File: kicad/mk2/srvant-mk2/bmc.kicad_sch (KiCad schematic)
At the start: 91 parts, among them J5 ARJM11, U13 KSZ9131RNXI-TR, U14 TPD4EUSB30, U15 TPD4EUSB30, Y2 25Mhz

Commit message: more progress
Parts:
- removed U12: ~, symbol custom-libraries:t113-s3
- added U4, U?: rp-t113-s3, rp-t113-s3:rp-t113-s3, symbol custom-libraries:t113-s3
- Y2: footprint srvant:LFXTAL-25MHz -> footprints:LFXTAL-25MHz; farnell# (none) -> 2854241; manf# (none) -> MCSJK-6F-25.00-20-30-40-B-50
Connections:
- net 3.3v: now also U4.30 (VCC-3V3)
- net EPHY_25M: now also U4.129 (EPHY_25M)
- net GND: now also U4.1 (GND), U4.105 (GND), U4.107 (GND), U4.109 (GND), U4.111 (GND), U4.114 (GND), U4.117 (GND), U4.134 (GND), U4.27 (GND), U4.29 (GND), U4.31 (GND), U4.33 (GND), U4.39 (GND), U4.56 (GND), U4.80 (GND), U4.87 (GND), U4.9 (GND), U4.90 (GND), U4.93 (GND), U4.99 (GND)
- net PHY_INT_N: now also U4.61 (PD_EINT4)
- net PHY_MDC: now also U4.119 (RMII-MDC)
- net PHY_MDIO: now also U4.118 (RMII-MDIO)
- net RESET_OUT_N: now also U4.60 (PD_EINT3)
- net RXC: now also U4.124 (RGMII_RXCK)
- net RXD0: now also U4.122 (RGMII_RXD0)
- net RXD1: now also U4.123 (RGMII_RXD1)
- net RXD2: now also U4.131 (RGMII_RXD2)
- net RXD3: now also U4.130 (RGMII_RXD3)
- net RX_CTL: now also U4.121 (RGMII_RXCTRL)
- net TXC: now also U4.125 (RGMII_TXCK)
- net TXD0: now also U4.126 (RGMII_TXD0)
- net TXD1: now also U4.127 (RGMII_TXD1)
- net TXD2: now also U4.133 (RGMII_TXD2)
- net TXD3: now also U4.132 (RGMII_TXD3)
- net TX_CTL: now also U4.128 (RGMII_TXCTRL)
- new net +5v: U4.28 (VSYS)
- new net BMC_DEBUG_RX: U?.63 (UART5_RX)
- new net BMC_DEBUG_TX: U?.62 (UART5_TX)
- new net BMC_I2C_0_SCK: U?.85 (TWI0_SCK)
- new net BMC_I2C_0_SDA: U?.86 (TWI0_SDA)
- new net BMC_I2C_1_SCK: U?.84 (TWI1_SCK)
- new net BMC_I2C_1_SDA: U?.83 (TWI1_SDA)
- new net BMC_I2C_2_SCK: U?.77 (TWI2_SCK)
- new net BMC_I2C_2_SDA: U?.78 (TWI2_SDA)
- new net BMC_I2C_3_SCK: U?.82 (TWI3_SCK)
- new net BMC_I2C_3_SDA: U?.81 (TWI3_SDA)
- new net BMC_UART0_RX: U?.52 (UART0_RX)
- new net BMC_UART0_TX: U?.53 (UART0_TX)
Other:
- moved on the sheet: C1, C9, D4, D5, FB6, J5, R4, U14, U15

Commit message: merge cm4 into one page, basic interconnection
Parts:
- gave numbers to parts that had none: 1
- renumbered C72 to C55, C71 to C56, D4 to D2, D5 to D3, FB3 to FB1, FB1 to FB3, FB6 to FB4, FB4 to FB5, FB5 to FB6, J5 to J2, TP8 to TP4, TP10 to TP5, TP11 to TP6, TP12 to TP7, TP13 to TP8, U4 to U3, U15 to U4, U14 to U5, U13 to U6, Y2 to Y1
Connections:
- net 3.3v renamed +3.3v

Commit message: more progress
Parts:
- removed TP8: TestPoint, TestPoint:TestPoint_Pad_D1.0mm, symbol ARJM11:TestPoint
- added C32, C9: 100n, Capacitor_SMD:C_0402_1005Metric, symbol Device:C
- added C33, C35, C36, C38, C39: 10u, Capacitor_SMD:C_0805_2012Metric, symbol Device:C
- added C34: 100u, Capacitor_Tantalum_SMD:CP_EIA-7343-31_Kemet-D, symbol Device:CP
- added D5 (x2): LED, LED_SMD:LED_0603_1608Metric, symbol Device:LED
- added FB1: 220R, Resistor_SMD:R_0402_1005Metric, symbol Device:FerriteBead_Small
- added J3: Conn_01x03, Connector_PinHeader_2.54mm:PinHeader_1x03_P2.54mm_Vertical, symbol Connector_Generic:Conn_01x03
- added J4: USB_OTG, Connector_USB:USB_Micro-B_Amphenol_10103594-0001LF_Horizontal, symbol Connector:USB_OTG
- added R10, R9: 3.3K, Resistor_SMD:R_0402_1005Metric, symbol Device:R
- added R15: 15K/1%, Resistor_SMD:R_0402_1005Metric, symbol Device:R
- added R16: 47K, Resistor_SMD:R_0402_1005Metric, symbol Device:R
- added R59 (x2): 1K, Resistor_SMD:R_0402_1005Metric, symbol Device:R
- added TP10: TestPoint, TestPoint:TestPoint_Pad_D1.0mm, symbol ARJM11:TestPoint
- added TP9 (x2): TestPoint, TestPoint:TestPoint_Pad_2.0x2.0mm, symbol Connector:TestPoint
- added U6: PCF85063AT/AAZ, Package_SO:SOIC-8_3.9x4.9mm_P1.27mm, symbol Timer_RTC:PCF8563T
- added U7: TPD4EUSB30, Package_SON:USON-10_2.5x1.0mm_P0.5mm, symbol CM4IO:TPD4EUSB30
- added U8: 74LVC2G07, Package_TO_SOT_SMD:SOT-23-6, symbol 74xGxx:74LVC2G07
- added U9: AP22653W6, Package_TO_SOT_SMD:SOT-23-6, symbol CM4IO:AP2553W6
- added Y1: X32K768S301, Crystal:Crystal_SMD_3215-2Pin_3.2x1.5mm, symbol Device:Crystal_Small
- renumbered C55 to C73, C56 to C74, D2 to D5, D3 to D6, FB1 to FB2, FB2 to FB3, FB3 to FB4, FB4 to FB5, FB5 to FB6, FB6 to FB7, J2 to J5, TP4 to TP6, TP5 to TP7, TP6 to TP8, TP7 to TP9, U4 to U10, U5 to U11, U6 to U12, U3 to U5, Y1 to Y2
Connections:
- net +3.3v: now also D5.2 (A); no longer FB6.2, FB7.2, U5.30 (VCC-3V3)
- net BMC_DEBUG_RX: now also J3.3 (Pin_3)
- net BMC_DEBUG_TX: now also J3.2 (Pin_2)
- net BMC_I2C_3_SCK: now also R9.1, U6.6 (SCL)
- net BMC_I2C_3_SDA: now also R10.1, U6.5 (SDA)
- net GND: now also C32.1, C33.2, C34.2, C35.2, C36.2, C38.2, C39.2, C9.2, FB1.1, J3.1 (Pin_1), R15.2, U6.4 (VSS), U7.3 (GND), U7.8 (GND), U8.2 (GND), U9.2 (GND)
- net PHY_AVDDH: now also TP10.1
- net BMC_USB_HOST_P: now reaches U5.112 (USB1-DP)
- net BMC_USB_HOST_N: now reaches U5.113 (USB1-DM)
- net BMC_USB_OTG_N: now reaches U5.115 (USB0-DM)
- net BMC_USB_OTG_N: now also J4.2 (D-), U7.5 (D2-), U7.6
- net BMC_USB_OTG_P: now reaches U5.116 (USB0-DP)
- net BMC_USB_OTG_P: now also J4.3 (D+), U7.4 (D2+), U7.7
- net BMC_HOST_POST_COMPLETE: now reaches U5.42 (PE_EINT13)
- net BMC_HOST_POWER_OUT: now reaches U5.43 (PE_EINT12)
- net BMC_HOST_RESET_OUT: now reaches U5.48 (PE_EINT7)
- net BMC_HOST_nRPIBOOT: now reaches U5.49 (PE_EINT6)
- net BMC_HOST_EEPROM_nWP: now reaches U5.50 (PE_EINT5)
- net BMC_HOST_USB_DEMUX_CONTROL: now reaches U5.51 (PE_EINT4)
- net BMC_HOST_POWER_EN: now reaches U5.54 (PE_EINT1)
- net BMC_HOST_WL_nDis: now reaches U5.55 (PE_EINT0)
- net BMC_ID_LED: now reaches U5.57 (PD_EINT0)
- net BMC_ID_LED: now also U8.3
- net BMC_POWER_LED: now reaches U5.66 (PD_EINT9)
- net BMC_POWER_LED: now also U8.1
- net BMC_SPI1_CS: now reaches U5.67 (SPI1_CS)
- net BMC_SPI1_CLK: now reaches U5.68 (SPI1_CLK)
- net BMC_SPI1_MOSI: now reaches U5.69 (SPI1_MOSI)
- net BMC_SPI1_MISO: now reaches U5.70 (SPI1_MISO)
- net BMC_USB_IDDET: now reaches U5.71 (USB_DET)
- net BMC_USB_IDDET: now also J4.4 (ID), R16.2
- net BMC_HOST_BT_nDis: now reaches U5.72 (PD_EINT15)
- net +5v renamed +5v_BMC
- net +5v_BMC: now also C33.1, U9.1 (IN)
- new net: FB1.2, J4.5 (GND), J4.6 (Shield)
- new net: R15.1, U9.5 (ILIM)
- new net: U6.2 (OSCO), Y1.1
- new net: U6.1 (OSCI), Y1.2
- new net: D5.1 (K), R59.1, TP9.1 (x2)
- new net: R59.2, U8.4
- new net: R59.2, U8.6
- new net: U7.1 (D1+), U7.10
- new net: U7.2 (D1-), U7.9
- new net +3.3v_BMC: C9.1, D5.2 (A), FB6.2, FB7.2, R10.2, R16.1, R9.2, U5.30 (VCC-3V3), U8.5 (VCC)
- new net +5V_OTG: C34.1, C35.1, C36.1, C38.1, C39.1, J4.1 (VBUS), U9.6 (OUT)
- new net +BATT: C32.2, U6.8 (VDD)
- new net NMI_N (XXX): U6.3 (~INT~)
- new net USB0_DRV: U9.3 (EN)
- new net USB0_nFAULT: U9.4 (nFault)
- no-connect marks 0 -> 16
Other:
- note added: "BMC RTC"
- note added: "CONECT ~INT (NMI_N) to the bmc"
- note added: "IIC address : 1010_001x"
- note added: "Micro USB ESD protection"
- note added: "TODO: connect nFault,IDDET,DRV in usb"
- note added: "USB OTG"
- note added: "required pins (buses): * uart for the debug * uart for the BMC->HOST communications * I2C for power measurements * I2C for BMC->HOST readings * I2C for temperature sensor * I2C for FAN control (could be the same as above) pins (IO) INPUT: * POST_COMPLETE (CM4 has started to boot) OUTPUT: * POWER_OUT (power cycle CM4) * RESET_OUT (reset CM4) * nRPIBOOT (force usb booting) * EEPROM_nWP (disable eep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"
- note added: "what are these keys?"
- note removed: "required pins (buses): * uart for the debug * uart for the BMC->HOST communications * I2C for power measurements * I2C for BMC->HOST readings * I2C for temperature sensor * I2C for FAN control (could be the same as above) pins (IO) INPUT: * BMC_POST_COMPLETE (CM4 has started to boot) OUTPUT: * BMC_POWER_OUT (power cycle CM4) * BMC_RESET_OUT (reset CM4) * BMC_nRPIBOOT (force usb booting) * BMC_EEP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"

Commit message: save state
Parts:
- removed C1 (x7): 10u/35v, Capacitor_SMD:C_0402_1005Metric, symbol Device:C
- removed C33, C35, C36, C38, C39: 10u, Capacitor_SMD:C_0805_2012Metric, symbol Device:C
- removed C34: 100u, Capacitor_Tantalum_SMD:CP_EIA-7343-31_Kemet-D, symbol Device:CP
- removed C73, C74: 15p, Capacitor_SMD:C_0402_1005Metric, symbol Device:C
- removed C9 (x26): 100n, Capacitor_SMD:C_0402_1005Metric, symbol Device:C
- removed D5, D6: 1N4148, Diode_SMD:D_SOD-523, symbol Diode:1N4148
- removed FB2, FB3, FB4, FB5, FB6, FB7: 220R, Resistor_SMD:R_0402_1005Metric, symbol Device:FerriteBead_Small
- removed J5: ARJM11, Connector_RJ:RJ45_Wuerth_7499111446_Horizontal, symbol Connector:ARJM11
- removed R15: 15K/1%, Resistor_SMD:R_0402_1005Metric, symbol Device:R
- removed R4 (x11): 1K, Resistor_SMD:R_0402_1005Metric, symbol Device:R
- removed R4 (x12): 22R, Resistor_SMD:R_0402_1005Metric, symbol Device:R
- removed R4 (x11): 10K, Resistor_SMD:R_0402_1005Metric, symbol Device:R
- removed R4 (x2): 330R, Resistor_SMD:R_0402_1005Metric, symbol Device:R
- removed R4: 6.04K, Resistor_SMD:R_0402_1005Metric, symbol Device:R
- removed TP10, TP6, TP7, TP8, TP9: TestPoint, TestPoint:TestPoint_Pad_D1.0mm, symbol ARJM11:TestPoint
- removed TP9 (x2): TestPoint, TestPoint:TestPoint_Pad_2.0x2.0mm, symbol Connector:TestPoint
- removed U10, U11: TPD4EUSB30, Package_SON:USON-10_2.5x1.0mm_P0.5mm, symbol CM4IO:TPD4EUSB30
- removed U12: KSZ9131RNXI-TR, KSZ9131RNXI-TR:QFN48_NX_MCH, symbol KSZ9131RNXI-TR:KSZ9131RNXI-TR
- removed unit 3 of U5
- removed U9: AP22653W6, Package_TO_SOT_SMD:SOT-23-6, symbol CM4IO:AP2553W6
- removed Y2: 25Mhz, footprints:LFXTAL-25MHz, symbol Device:Crystal_GND24
- added C9: 100n, Capacitor_SMD:C_0402_1005Metric, symbol Device:C
- added D9: PESD2USB5UX-T, Package_TO_SOT_SMD:SOT-23, symbol Power_Protection:SP0502BAHT
- added J6: Conn_02x05_Odd_Even, Connector_PinHeader_2.54mm:PinHeader_2x05_P2.54mm_Vertical, symbol Connector_Generic:Conn_02x05_Odd_Even
- added R10, R9: 3.3K, Resistor_SMD:R_0402_1005Metric, symbol Device:R
- added R53 (x6): 0, Resistor_SMD:R_0402_1005Metric, symbol Device:R
- added SW1: POWER, footprints:button-SW_TL3340AF160QG, symbol Switch:SW_Push
- added SW2: EMMC_KEY, button-1571563-4:SW4_FSM-5P23_TEC, symbol Switch:SW_Push
- added SW3: RST, button-1571563-4:SW4_FSM-5P23_TEC, symbol Switch:SW_Push
- added SW4: HOST_RESET, footprints:button-SW_TL3340AF160QG, symbol Switch:SW_Push
- added TP17: 5v OTG, TestPoint:TestPoint_Pad_D1.0mm, symbol ARJM11:TestPoint
- added TP3: NMI_N, TestPoint:TestPoint_Pad_D1.0mm, symbol Connector:TestPoint
- added TP3: GND, TestPoint:TestPoint_Pad_D1.0mm, symbol Connector:TestPoint
- added TP5: 3.3v BMC, TestPoint:TestPoint_Pad_D1.0mm, symbol ARJM11:TestPoint
- added U22: TMP1075DSG, Package_SON:WSON-8-1EP_2x2mm_P0.5mm_EP0.9x1.6mm_ThermalVias, symbol Sensor_Temperature:TMP1075DSG
- added U25: 74AHC1G08, Package_TO_SOT_SMD:SOT-23-5, symbol 74xGxx:74AHC1G08
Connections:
- net +3.3v is gone; now on net +3.3v_BMC: D5.2 (A)
- net +3.3v_BMC: now also C9.1, J6.3 (Pin_3), R10.2, R9.2, SW2.2, TP5.1, U22.8 (V+)
- net +5v_BMC: now also U5.36 (POWER_EN), J6.1 (Pin_1), U25.5 (VCC)
- net BMC_HOST_EEPROM_nWP: now also R53.1; no longer U5.50 (PE_EINT5)
- net BMC_HOST_POST_COMPLETE: now also U5.75 (PWM2); no longer U5.42 (PE_EINT13)
- net BMC_HOST_POWER_EN: now also R53.1; no longer U5.54 (PE_EINT1)
- net BMC_HOST_POWER_OUT: now also U5.76 (PWM3); no longer U5.43 (PE_EINT12)
- net BMC_HOST_RESET_OUT: now also R53.1; no longer U5.48 (PE_EINT7)
- net BMC_HOST_USB_DEMUX_CONTROL: now also U5.50 (PE_EINT5); no longer U5.51 (PE_EINT4)
- net BMC_HOST_WL_nDis: now also R53.1; no longer U5.55 (PE_EINT0)
- net BMC_HOST_nRPIBOOT: now also R53.1; no longer U5.49 (PE_EINT6)
- net BMC_I2C_2_SCK: now also J6.5 (Pin_5), R9.1, U22.2 (SCL)
- net BMC_I2C_2_SDA: now also J6.7 (Pin_7), R10.1, U22.1 (SDA)
- net BMC_ID_LED: now also U5.74 (PWM1); no longer U5.57 (PD_EINT0)
- net BMC_POWER_LED: now also U5.73 (PWM0); no longer U5.66 (PD_EINT9)
- net BMC_SPI1_CLK: now also J6.4 (Pin_4)
- net BMC_SPI1_CS: now also J6.2 (Pin_2)
- net BMC_SPI1_MISO: now also J6.8 (Pin_8)
- net BMC_SPI1_MOSI: now also J6.6 (Pin_6)
- net GND: now also C9.2, D9.3 (A), J6.10 (Pin_10), J6.9 (Pin_9), SW1.2, SW3.1, SW4.2, TP3.1, U22.4 (GND), U22.5 (A2), U22.6 (A1), U22.7 (A0), U22.9 (EP), U25.3 (GND)
- net BMC_UART1_RX: now reaches U5.44 (UART1_RX)
- net BMC_UART1_TX: now reaches U5.45 (UART1_TX)
- net BMC_TEMP_ALERT: now reaches U5.79 (PWM7)
- net BMC_TEMP_ALERT: now also U22.3 (ALERT)
- net EMMC_KEY: now reaches U5.35 (EMMC_KEY)
- net EMMC_KEY: now also D9.1 (K), SW2.1
- net RST_KEY: now reaches U5.37 (KEY_RST)
- net RST_KEY: now also D9.2 (K), U25.4
- net +5V_OTG renamed +5V_BMC_OTG
- net +5V_BMC_OTG: now also TP17.1
- net NMI_N (XXX) renamed NMI_N
- net NMI_N: now also R53.2, TP3.1
- new net: R53.2, U5.48 (PE_EINT7)
- new net: R53.2, U5.49 (PE_EINT6)
- new net: R53.2, U5.54 (PE_EINT1)
- new net: R53.2, U5.51 (PE_EINT4)
- new net: SW3.2, U25.1
- new net: R53.1, U25.2
- new net: R53.2, U5.55 (PE_EINT0)
- new net BMC_HOST_POWER_BUTTON: SW1.1, U5.42 (PE_EINT13)
- new net BMC_HOST_RESET_BUTTON: SW4.1, U5.43 (PE_EINT12)
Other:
- note added: "+VBUS(5V_BMC_OTG): where to connect in client-only mode?"
- note added: "BMC_HOST_USB_DEMUX_CONTROL: * switches usb MUX for HOST to go into client mode"
- note added: "DEV INTERFACE * I2C is shared with temp sensor"
- note added: "EMMC_KEY: upgrade pin/button"
- note added: "ESD protection (TVS diod) dual channel, to protect both EMMC_KEY and RST_KEY"
- note added: "Even though t113 has onboard RTC, it seems like rp-t113 doesn't expose RTC-POWER pin and overall they use i2c rtc on their reference board."
- note added: "RST_KEY: driving it low will reset the BMC. use AND gate with inputs from the button and RTC"
- note added: "TMP1075 temperature sensor"
- note added: "interrupt to rest BMC, also add TestPad for wire soldering"
- note added: "pin35 - EMMC_KEY: 1v8-3v3 - input - upgrade button pin36 - POWER_EN: 3v4-5v5 - input - boot enabled pin37 - KEY_RST: 3v3 - input - reset button pin100 - GPADC0: 1V8 - input - Analog ADC input"
- note added: "power: 5V 500mA"
- note removed: "125MHz output PU = enable PD = disable"
- note removed: "CONECT ~INT (NMI_N) to the bmc"
- note removed: "Mode [3:0] Description 1000 10/100 Full and Half, 1000BT Full (RGMII), PME Enable on LED1 1010 10/100 Full and Half, 1000BT Full (RGMII), PME Enable on INT_N 1100 1000BT Full (RGMII) 1110 10/100 Full and Half, 1000BT Full (RGMII)"
- note removed: "PHY ADDRESS = 03h"
- note removed: "PU = Single LED mode PD = Tricolor mode"
- note removed: "Place these 22R resistors as close as possible to KSZ9131"
- note removed: "Place these 22R resistors as close as possible to MAC"
- note removed: "RGMII_CLKIN: function unknown possibly needs to be connected to CLK125 of PHY"
- note removed: "TODO: 1) RESET PIN datasheet [1] page 138 [1] - https://ww1.microchip.com/downloads/aemDocuments/documents/UNG/ProductDocuments/DataSheets/00002841D.pdf [2] - https://ww1.microchip.com/downloads/en/DeviceDoc/KSZ9131RNX-Hardware-Design-Checklist-00003370A.pdf 2) EPHY_25M decide whether to use 25M generated by CPU or to use external XTAL"
- note removed: "TODO: connect nFault,IDDET,DRV in usb"
- note removed: "The INT_N pin is an optional interrupt signal that is used to inform the external controller that there has been a status update in the KSZ9131RNX PHY register."
- note removed: "USB OTG"
- note removed: "internal LDO (LDO_0) produces +1.2V. even though the reference design [1] suggests the use of external LDO, the following doc [2] describes both approaches (even though it's not specifically for this chip) [1] - https://ww1.microchip.com/downloads/en/DeviceDoc/KSZ9131RNX%20Reference%20Design.pdf [2] - https://microchip.my.site.com/s/article/How-to-Use-Internal-LDO-Correctly-in-the-KSZ8873-KSZ8863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"
- note removed: "what are these keys?"
- moved on the sheet: C32, C9, D5, FB1, J3, J4, R10, R16, R59, R9, U5A, U5B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

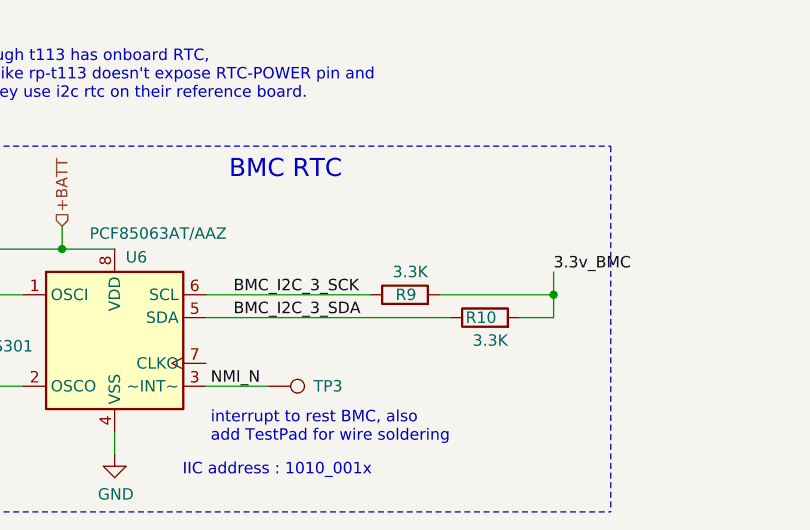
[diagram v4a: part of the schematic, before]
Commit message: mostly wired, impedance control, etc
Repositioned most of the components. Set impedance control based
on jlcpcb calculator.

Need to:
* reposition ethernet port to allow mounting hole.
* move power socket lower, reduce board size
* fix the rest of DRC errors.
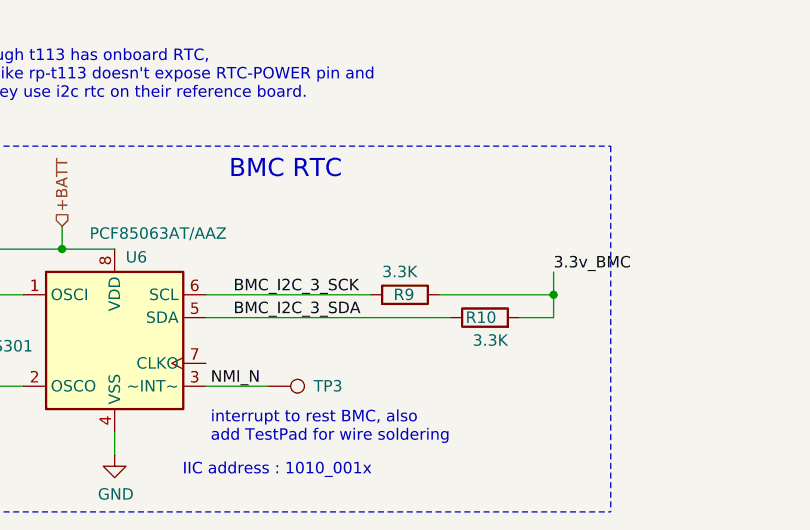
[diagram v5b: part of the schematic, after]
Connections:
- net +3.3v_BMC: now also R9.1; no longer R9.2
- net BMC_I2C_3_SCK: now also R9.2; no longer R9.1
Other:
- moved on the sheet: R9
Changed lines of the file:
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@@
     )
   )
-  (symbol (lib_id "Device:R") (at 86.36 252.73 90) (unit 1)
+  (symbol (lib_id "Device:R") (at 86.36 252.73 270) (mirror x) (unit 1)
     (in_bom yes) (on_board yes) (dnp no)
-    (property "Reference" "R9" (at 87.63 252.73 90)
+    (property "Reference" "R9" (at 85.09 252.73 90)
       (effects (font (size 1.27 1.27)) (justify left))
     )
-    (property "Value" "3.3K" (at 88.9 250.19 90)
+    (property "Value" "3.3K" (at 83.82 250.19 90)
       (effects (font (size 1.27 1.27)) (justify left))
     )

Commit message: fix descriptions, add 3dmodels.
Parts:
- C32, C9: Part Description 0.1uF 10% 16V Ceramic Capacitor X7R 0402 (1005 Metric) -> 0.1uF 10% 16V Ceramic Capacitor X7R 0402 (1005 Metric)
- D5: Part Description Red 620nm LED Indication - Discrete 2.2V 2-SMD, No Lead -> Red 620nm LED Indication - Discrete 2.2V 2-SMD, No Lead
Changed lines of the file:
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@@
       (effects (font (size 1.27 1.27)) hide)
     )
-    (property "Datasheet" "https://search.murata.co.jp/Ceramy/image/img/A01X/G101/ENG/GRM155R71C104KA88-01.pdf" (at 393.7 33.02 0)
-      (effects (font (size 1.27 1.27)) hide)
-    )
-    (property "Part Description" "	0.1uF 10% 16V Ceramic Capacitor X7R 0402 (1005 Metric)" (at 393.7 33.02 0)
+    (property "Datasheet" "SRN4018-4R7M" (at 393.7 33.02 0)
+      (effects (font (size 1.27 1.27)) hide)
+    )
+    (property "Part Description" "0.1uF 10% 16V Ceramic Capacitor X7R 0402 (1005 Metric)" (at 393.7 33.02 0)
       (effects (font (size 1.27 1.27)) hide)
     )
@@
       (effects (font (size 1.27 1.27)) hide)
     )
-    (property "Datasheet" "https://search.murata.co.jp/Ceramy/image/img/A01X/G101/ENG/GRM155R71C104KA88-01.pdf" (at 35.052 247.65 0)
+    (property "Datasheet" "SRN4018-4R7M" (at 35.052 247.65 0)
       (effects (font (size 1.27 1.27)) hide)
     )
@@
       (effects (font (size 1.27 1.27)) hide)
     )
-    (property "Part Description" "	0.1uF 10% 16V Ceramic Capacitor X7R 0402 (1005 Metric)" (at 35.052 247.65 0)
+    (property "Part Description" "0.1uF 10% 16V Ceramic Capacitor X7R 0402 (1005 Metric)" (at 35.052 247.65 0)
       (effects (font (size 1.27 1.27)) hide)
     )
@@
       (effects (font (size 1.27 1.27)) hide)
     )
-    (property "Part Description" "	Red 620nm LED Indication - Discrete 2.2V 2-SMD, No Lead" (at 226.06 50.8 0)
+    (property "Part Description" "Red 620nm LED Indication - Discrete 2.2V 2-SMD, No Lead" (at 226.06 50.8 0)
       (effects (font (size 1.27 1.27)) hide)
     )
@@
       (effects (font (size 1.27 1.27)) hide)
     )
-    (property "Part Description" "	Red 620nm LED Indication - Discrete 2.2V 2-SMD, No Lead" (at 226.06 33.02 0)
+    (property "Part Description" "Red 620nm LED Indication - Discrete 2.2V 2-SMD, No Lead" (at 226.06 33.02 0)
       (effects (font (size 1.27 1.27)) hide)
     )
@@
       (effects (font (size 1.27 1.27)) hide)
     )
-    (property "Datasheet" "https://search.murata.co.jp/Ceramy/image/img/A01X/G101/ENG/GRM155R71C104KA88-01.pdf" (at 245.11 45.72 0)
-      (effects (font (size 1.27 1.27)) hide)
-    )
-    (property "Part Description" "	0.1uF 10% 16V Ceramic Capacitor X7R 0402 (1005 Metric)" (at 245.11 45.72 0)
-      (effects (font (size 1.27 1.27)) hide)
-    )
+    (property "Datasheet" "SRN4018-4R7M" (at 245.11 45.72 0)
+      (effects (font (size 1.27 1.27)) hide)
+    )
+    (property "Part Description" "0.1uF 10% 16V Ceramic Capacitor X7R 0402 (1005 Metric)" (at 245.11 45.72 0)
+      (effects (font (size 1.27 1.27)) hide)
+    )
